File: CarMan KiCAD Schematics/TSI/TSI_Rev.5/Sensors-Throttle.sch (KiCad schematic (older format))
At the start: 54 parts, among them IC2 TS431ILT, U21 MCP6004, U25 NCD9830DBR2G, U26 MCP6004, U4 ACPL-C870, U40 MCP6004, U5 SI8600AB-B-IS

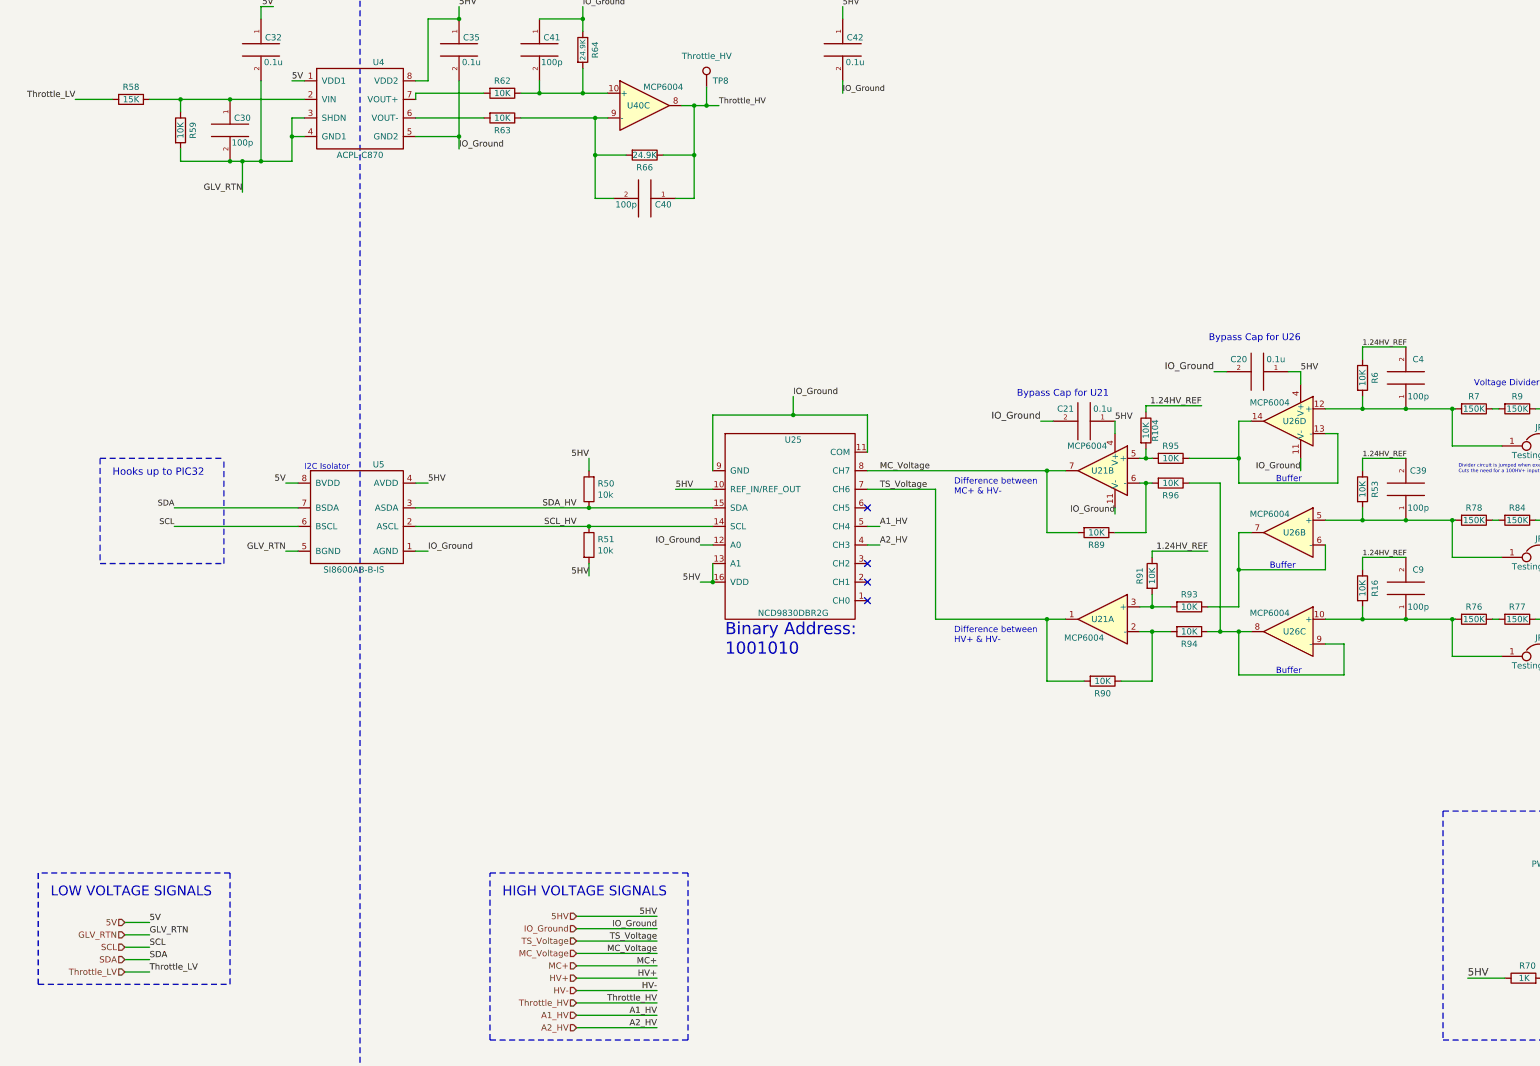
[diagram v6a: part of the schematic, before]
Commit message: - Removed capacitors across R16, R53, R6 - Capacitive load was too much for 1.24HV Ref - Notes on Pre-charge circuit & Throttle Plausibility - Cooling, Relays & Voltage Refs
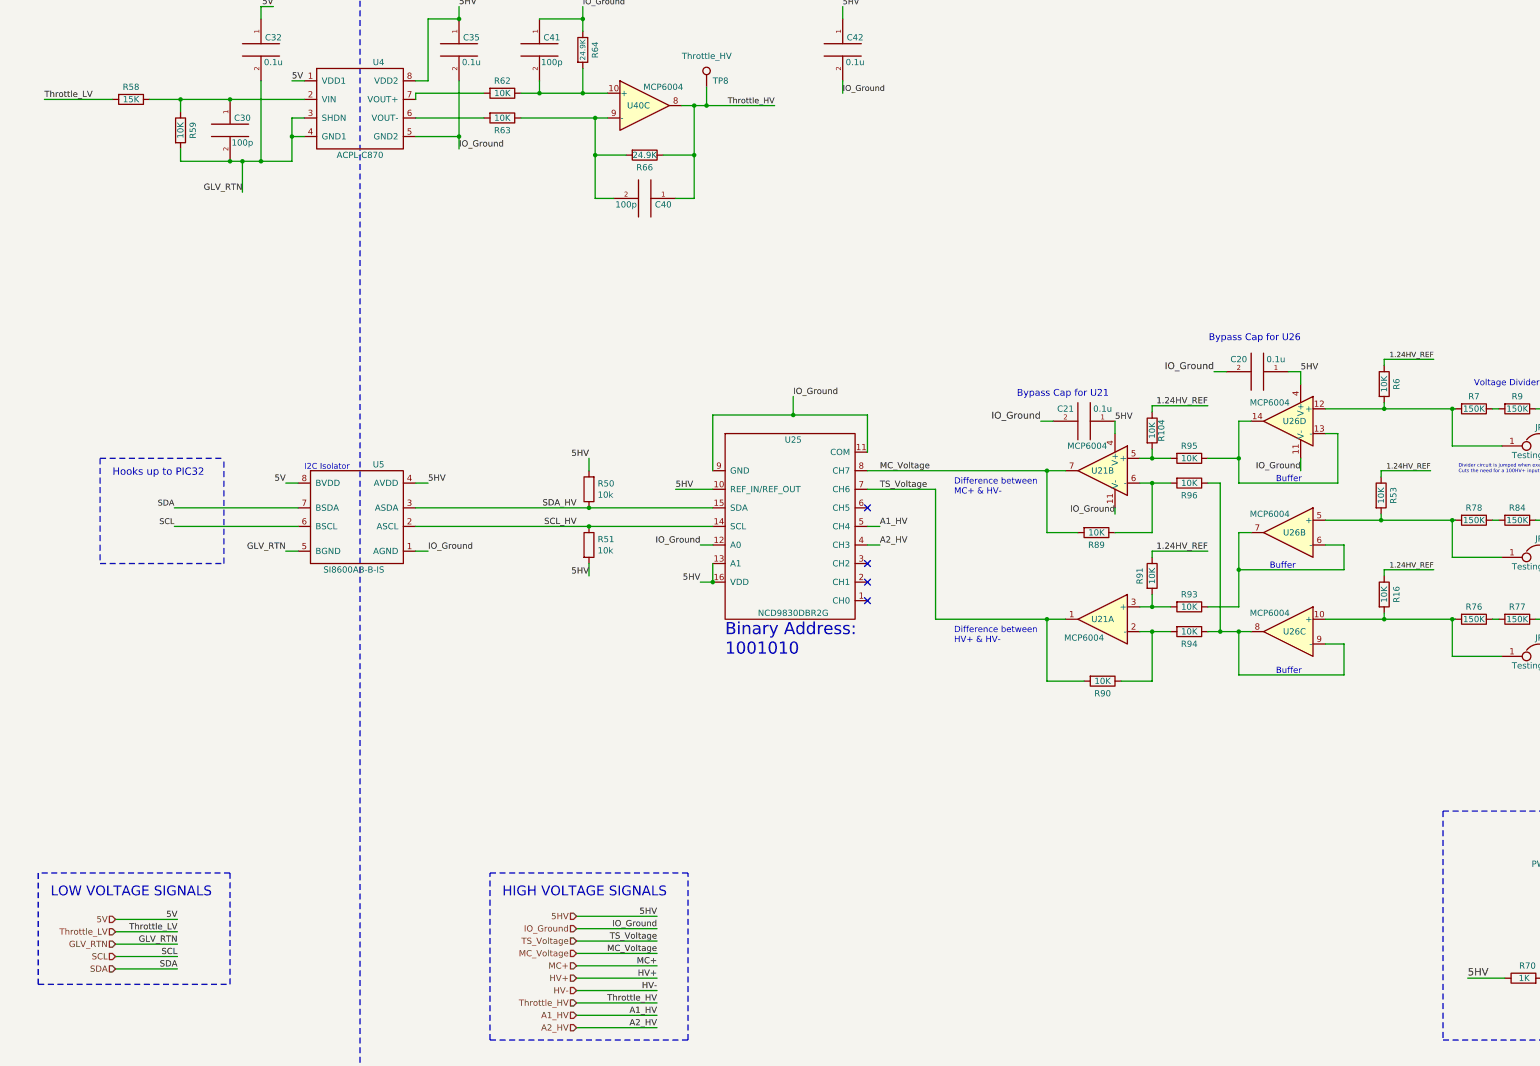
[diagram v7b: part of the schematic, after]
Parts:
- removed C39, C4, C9: 100p, Capacitor_SMD:C_0805_2012Metric_Pad1.15x1.40mm_HandSolder, symbol pspice:CAP
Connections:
- wire segments 205 -> 203
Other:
- moved on the sheet: R104, R16, R95, R96

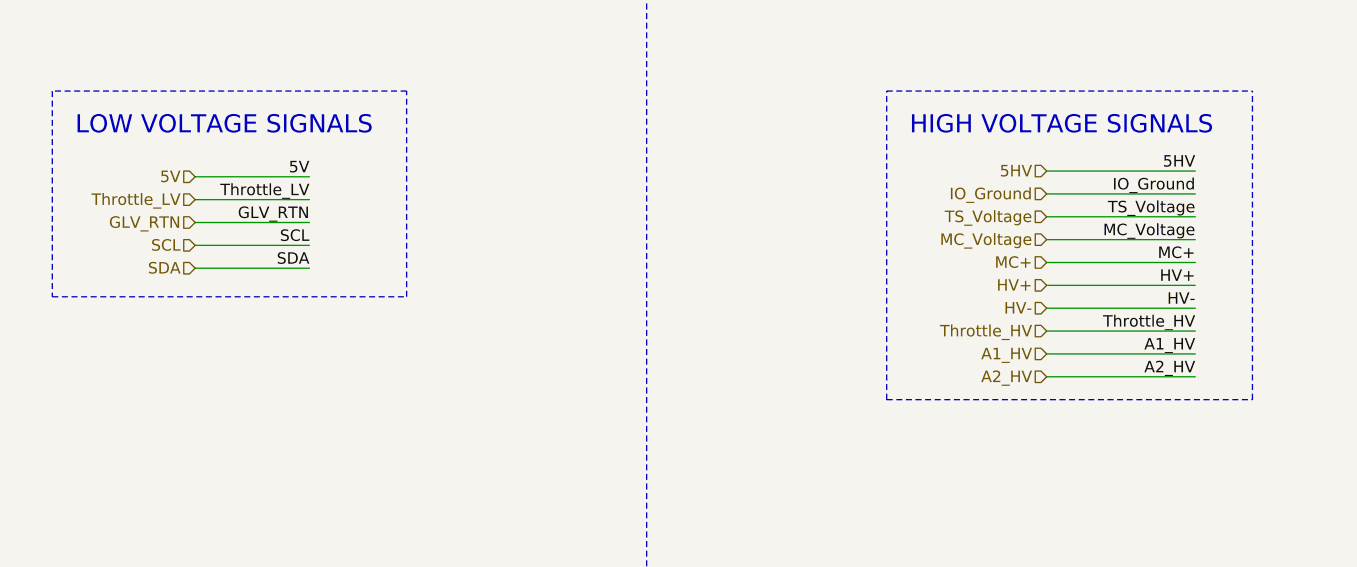
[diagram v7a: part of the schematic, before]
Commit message: General signal directions -> i/o
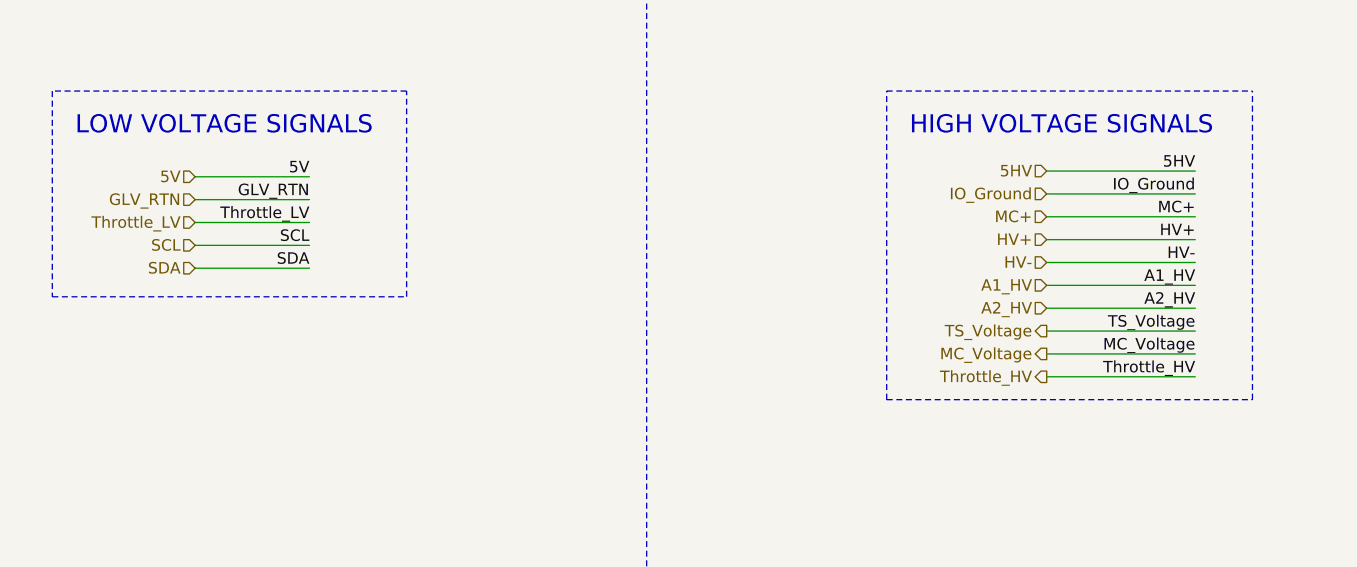
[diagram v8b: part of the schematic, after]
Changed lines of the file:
@@
 $Descr A3 16535 11693
 encoding utf-8
-Sheet 6 6
+Sheet 4 6
 Title ""
 Date ""
@@
 Text HLabel 5750 8700 0    50   Input ~ 0
 5HV
-Text HLabel 5750 9400 0    50   Input ~ 0
+Text HLabel 5750 9600 0    50   Output ~ 0
 Throttle_HV
 Text Label 6400 8800 2    50   ~ 0
 IO_Ground
-Text Label 6400 9400 2    50   ~ 0
+Text Label 6400 9600 2    50   ~ 0
 Throttle_HV
 Text Label 6400 8700 2    50   ~ 0
@@
 Text Notes 5150 8550 0    79   ~ 0
 HIGH VOLTAGE SIGNALS\n
-Text Label 6400 9200 2    50   ~ 0
+Text Label 6400 9000 2    50   ~ 0
 HV+
+Text Label 6400 9400 2    50   ~ 0
+TS_Voltage
 Text Label 6400 8900 2    50   ~ 0
+MC+
+Text HLabel 5750 9400 0    50   Output ~ 0
 TS_Voltage
+Text HLabel 5750 8900 0    50   Input ~ 0
+MC+
+Text HLabel 5750 9000 0    50   Input ~ 0
+HV+
 Text Label 6400 9100 2    50   ~ 0
-MC+
-Text HLabel 5750 8900 0    50   Input ~ 0
-TS_Voltage
+HV-
 Text HLabel 5750 9100 0    50   Input ~ 0
-MC+
-Text HLabel 5750 9200 0    50   Input ~ 0
-HV+
-Text Label 6400 9300 2    50   ~ 0
-HV-
-Text HLabel 5750 9300 0    50   Input ~ 0
 HV-
 Wire Wire Line
@@
 Text Notes 12200 10350 0    157  ~ 0
 THROTTLE VOLTAGE ISOLATOR
-Text Label 6400 9600 2    50   ~ 0
+Text Label 6400 9300 2    50   ~ 0
 A2_HV
-Text Label 6400 9500 2    50   ~ 0
+Text Label 6400 9200 2    50   ~ 0
 A1_HV
-Text HLabel 5750 9500 0    50   Input ~ 0
+Text HLabel 5750 9200 0    50   Input ~ 0
 A1_HV
-Text HLabel 5750 9600 0    50   Input ~ 0
+Text HLabel 5750 9300 0    50   Input ~ 0
 A2_HV
 $Comp
@@
 Wire Wire Line
 	3300 1350 3200 1350
-Text Label 6400 9000 2    50   ~ 0
+Text Label 6400 9500 2    50   ~ 0
 MC_Voltage
-Text HLabel 5750 9000 0    50   Input ~ 0
+Text HLabel 5750 9500 0    50   Output ~ 0
 MC_Voltage
 $Comp
@@
 	6550 5250 6850 5250
 Wire Wire Line
+	5750 9400 6400 9400
+Wire Wire Line
+	5750 8700 6400 8700
+Wire Wire Line
+	5750 8800 6400 8800
+Wire Wire Line
+	5750 9000 6400 9000
+Wire Wire Line
+	5750 9500 6400 9500
+Wire Wire Line
 	5750 8900 6400 8900
 Wire Wire Line
-	5750 8700 6400 8700
-Wire Wire Line
-	5750 8800 6400 8800
-Wire Wire Line
 	5750 9200 6400 9200
 Wire Wire Line
-	5750 9000 6400 9000
-Wire Wire Line
 	5750 9100 6400 9100
 Wire Wire Line
-	5750 9500 6400 9500
+	5750 9600 6400 9600
 Wire Wire Line
 	5750 9300 6400 9300
-Wire Wire Line
-	5750 9400 6400 9400
-Wire Wire Line
-	5750 9600 6400 9600
 Wire Notes Line
 	2950 9250 2950 8350
@@
 	12750 7850 12750 9700
 Wire Wire Line
+	2025 8925 2525 8925
+Wire Wire Line
+	2025 8725 2525 8725
+Wire Wire Line
 	2025 8825 2525 8825
 Wire Wire Line
-	2025 8725 2525 8725
-Wire Wire Line
-	2025 8925 2525 8925
-Wire Wire Line
 	2025 9025 2525 9025
 Wire Wire Line
 	2025 9125 2525 9125
-Text HLabel 2025 8825 0    50   Input ~ 0
+Text HLabel 2025 8925 0    50   Input ~ 0
 Throttle_LV
 Text HLabel 2025 9025 0    50   Input ~ 0
@@
 Text HLabel 2025 8725 0    50   Input ~ 0
 5V
-Text HLabel 2025 8925 0    50   Input ~ 0
+Text HLabel 2025 8825 0    50   Input ~ 0
 GLV_RTN
 Text Label 2525 8725 2    50   ~ 0
 5V
+Text Label 2525 8925 2    50   ~ 0
+Throttle_LV
 Text Label 2525 8825 2    50   ~ 0
-Throttle_LV
-Text Label 2525 8925 2    50   ~ 0
 GLV_RTN
 Wire Wire Line
